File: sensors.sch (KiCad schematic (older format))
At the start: 14 parts, among them Q1901 FDV301N, Q1902 FDV301N, U1901 RPR-0521RS, U1902 ICM-20948

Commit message: Modify the boot config/boot mode pins and switch such that only eMMC and USB (serial downloader) are boot options due to the uSD being attached to the USB<->SD bridge chip, add OV5460 notes about using the internal DVDD 1.5V regulator
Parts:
- renumbered C1901 to C2001, C1902 to C2002, C1903 to C2003, C1904 to C2004, C1905 to C2005, C1906 to C2006, Q1901 to Q2001, Q1902 to Q2002, R1901 to R2001, R1902 to R2002, R1903 to R2003, R1904 to R2004, U1901 to U2001, U1902 to U2002
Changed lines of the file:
@@
 $EndDescr
 $Comp
-L R R1902
+L R R2002
 U 1 1 5B0661C0
 P 4150 2150
-F 0 "R1902" V 4230 2150 50  0000 C CNN
+F 0 "R2002" V 4230 2150 50  0000 C CNN
 F 1 "22" V 4150 2150 50  0000 C CNN
 F 2 "Resistors_SMD:R_0603" V 4080 2150 50  0001 C CNN
@@
 $EndComp
 $Comp
-L C C1903
+L C C2003
 U 1 1 5B067A54
 P 4700 3150
-F 0 "C1903" H 4725 3250 50  0000 L CNN
+F 0 "C2003" H 4725 3250 50  0000 L CNN
 F 1 "100nF" H 4725 3050 50  0000 L CNN
 F 2 "" H 4738 3000 50  0001 C CNN
@@
 	4400 3500 4350 3500
 $Comp
-L GND #PWR0311
+L GND #PWR0305
 U 1 1 5B067AE0
 P 4600 3400
-F 0 "#PWR0311" H 4600 3150 50  0001 C CNN
+F 0 "#PWR0305" H 4600 3150 50  0001 C CNN
 F 1 "GND" H 4600 3250 50  0000 C CNN
 F 2 "" H 4600 3400 50  0001 C CNN
@@
 	4700 2950 4350 2950
 $Comp
-L GND #PWR0312
+L GND #PWR0306
 U 1 1 5B068781
 P 3800 4000
-F 0 "#PWR0312" H 3800 3750 50  0001 C CNN
+F 0 "#PWR0306" H 3800 3750 50  0001 C CNN
 F 1 "GND" H 3800 3850 50  0000 C CNN
 F 2 "" H 3800 4000 50  0001 C CNN
@@
 	3800 4000 3800 3950
 $Comp
-L GND #PWR0313
+L GND #PWR0307
 U 1 1 5B068863
 P 3600 2550
-F 0 "#PWR0313" H 3600 2300 50  0001 C CNN
+F 0 "#PWR0307" H 3600 2300 50  0001 C CNN
 F 1 "GND" H 3600 2400 50  0000 C CNN
 F 2 "" H 3600 2550 50  0001 C CNN
@@
 Connection ~ 3800 2150
 $Comp
-L 3V3_P #PWR0314
+L 3V3_P #PWR0308
 U 1 1 5B0689D2
 P 4700 2100
-F 0 "#PWR0314" H 4700 1950 50  0001 C CNN
+F 0 "#PWR0308" H 4700 1950 50  0001 C CNN
 F 1 "3V3_P" H 4700 2240 50  0000 C CNN
 F 2 "" H 4700 2100 50  0001 C CNN
@@
 	3250 2950 2750 2950
 $Comp
-L 3V3_P #PWR0315
+L 3V3_P #PWR0309
 U 1 1 5B069B9B
 P 3200 2900
-F 0 "#PWR0315" H 3200 2750 50  0001 C CNN
+F 0 "#PWR0309" H 3200 2750 50  0001 C CNN
 F 1 "3V3_P" H 3200 3040 50  0000 C CNN
 F 2 "" H 3200 2900 50  0001 C CNN
@@
 Proximity & Ambient Light
 $Comp
-L RPR-0521RS U1901
+L RPR-0521RS U2001
 U 1 1 5B0DE7C1
 P 3800 3300
-F 0 "U1901" H 3600 3800 60  0000 C CNN
+F 0 "U2001" H 3600 3800 60  0000 C CNN
 F 1 "RPR-0521RS" H 4100 3800 60  0000 C CNN
 F 2 "dvk-mx8m-bsb:RPR-0521RS" H 3800 3150 60  0001 C CNN
@@
 $EndComp
 $Comp
-L C C1902
+L C C2002
 U 1 1 5B0E0E47
 P 4500 3150
-F 0 "C1902" H 4525 3250 50  0000 L CNN
+F 0 "C2002" H 4525 3250 50  0000 L CNN
 F 1 "100nF" H 4525 3050 50  0000 L CNN
 F 2 "" H 4538 3000 50  0001 C CNN
@@
 	7450 2400 6800 2400
 $Comp
-L GND #PWR0316
+L GND #PWR0310
 U 1 1 5B0EFE3A
 P 7300 2650
-F 0 "#PWR0316" H 7300 2400 50  0001 C CNN
+F 0 "#PWR0310" H 7300 2400 50  0001 C CNN
 F 1 "GND" H 7300 2500 50  0000 C CNN
 F 2 "" H 7300 2650 50  0001 C CNN
@@
 Reference:\nhttps://store.invensense.com/datasheets/invensense/\nAN-IVS-0001EVB-00%20v1%202.pdf
 $Comp
-L C C1906
+L C C2006
 U 1 1 5B0F1B79
 P 9450 2300
-F 0 "C1906" H 9475 2400 50  0000 L CNN
+F 0 "C2006" H 9475 2400 50  0000 L CNN
 F 1 "100nF" H 9475 2200 50  0000 L CNN
 F 2 "" H 9488 2150 50  0001 C CNN
@@
 	8750 2100 9450 2100
 $Comp
-L GND #PWR0317
+L GND #PWR0311
 U 1 1 5B0F1D3B
 P 9450 2500
-F 0 "#PWR0317" H 9450 2250 50  0001 C CNN
+F 0 "#PWR0311" H 9450 2250 50  0001 C CNN
 F 1 "GND" H 9450 2350 50  0000 C CNN
 F 2 "" H 9450 2500 50  0001 C CNN
@@
 	9450 2500 9450 2450
 $Comp
-L 3V3_P #PWR0318
+L 3V3_P #PWR0312
 U 1 1 5B0F3735
 P 9450 2050
-F 0 "#PWR0318" H 9450 1900 50  0001 C CNN
+F 0 "#PWR0312" H 9450 1900 50  0001 C CNN
 F 1 "3V3_P" H 9450 2190 50  0000 C CNN
 F 2 "" H 9450 2050 50  0001 C CNN
@@
 Connection ~ 9450 2100
 $Comp
-L 1V8_P #PWR0319
+L 1V8_P #PWR0313
 U 1 1 5B0F45AF
 P 6700 2050
-F 0 "#PWR0319" H 6700 1900 50  0001 C CNN
+F 0 "#PWR0313" H 6700 1900 50  0001 C CNN
 F 1 "1V8_P" H 6700 2190 50  0000 C CNN
 F 2 "" H 6700 2050 50  0001 C CNN
@@
 $EndComp
 $Comp
-L C C1904
+L C C2004
 U 1 1 5B0F45D3
 P 6700 2450
-F 0 "C1904" H 6725 2550 50  0000 L CNN
+F 0 "C2004" H 6725 2550 50  0000 L CNN
 F 1 "100nF" H 6725 2350 50  0000 L CNN
 F 2 "" H 6738 2300 50  0001 C CNN
@@
 $EndComp
 $Comp
-L GND #PWR0320
+L GND #PWR0314
 U 1 1 5B0F4626
 P 6700 2650
-F 0 "#PWR0320" H 6700 2400 50  0001 C CNN
+F 0 "#PWR0314" H 6700 2400 50  0001 C CNN
 F 1 "GND" H 6700 2500 50  0000 C CNN
 F 2 "" H 6700 2650 50  0001 C CNN
@@
 	6700 2650 6700 2600
 $Comp
-L C C1905
+L C C2005
 U 1 1 5B0FA115
 P 9050 2800
-F 0 "C1905" H 9075 2900 50  0000 L CNN
+F 0 "C2005" H 9075 2900 50  0000 L CNN
 F 1 "100nF" H 9075 2700 50  0000 L CNN
 F 2 "" H 9088 2650 50  0001 C CNN
@@
 $EndComp
 $Comp
-L GND #PWR0321
+L GND #PWR0315
 U 1 1 5B0FA198
 P 9050 3000
-F 0 "#PWR0321" H 9050 2750 50  0001 C CNN
+F 0 "#PWR0315" H 9050 2750 50  0001 C CNN
 F 1 "GND" H 9050 2850 50  0000 C CNN
 F 2 "" H 9050 3000 50  0001 C CNN
@@
 	9050 3000 9050 2950
 $Comp
-L 1V8_P #PWR0322
+L 1V8_P #PWR0316
 U 1 1 5B0FDFE1
 P 8800 2050
-F 0 "#PWR0322" H 8800 1900 50  0001 C CNN
+F 0 "#PWR0316" H 8800 1900 50  0001 C CNN
 F 1 "1V8_P" H 8800 2190 50  0000 C CNN
 F 2 "" H 8800 2050 50  0001 C CNN
@@
 	7450 2500 7400 2500
 $Comp
-L GND #PWR0323
+L GND #PWR0317
 U 1 1 5B105474
 P 8850 2650
-F 0 "#PWR0323" H 8850 2400 50  0001 C CNN
+F 0 "#PWR0317" H 8850 2400 50  0001 C CNN
 F 1 "GND" H 8850 2500 50  0000 C CNN
 F 2 "" H 8850 2650 50  0001 C CNN
@@
 I2C's VIH=1.8V
 $Comp
-L Q_NMOS_SGD Q1901
+L Q_NMOS_SGD Q2001
 U 1 1 5B11E6E9
 P 4500 5450
-F 0 "Q1901" V 4750 5350 50  0000 L CNN
+F 0 "Q2001" V 4750 5350 50  0000 L CNN
 F 1 "FDV301N" V 4850 5300 50  0000 L CNN
 F 2 "" H 4700 5550 50  0001 C CNN
@@
 $EndComp
 $Comp
-L 1V8_P #PWR0324
+L 1V8_P #PWR0318
 U 1 1 5B11E6F7
 P 4750 5100
-F 0 "#PWR0324" H 4750 4950 50  0001 C CNN
+F 0 "#PWR0318" H 4750 4950 50  0001 C CNN
 F 1 "1V8_P" H 4750 5240 50  0000 C CNN
 F 2 "" H 4750 5100 50  0001 C CNN
@@
 Connection ~ 4750 5150
 $Comp
-L Q_NMOS_SGD Q1902
+L Q_NMOS_SGD Q2002
 U 1 1 5B11E705
 P 6800 5450
-F 0 "Q1902" V 7050 5350 50  0000 L CNN
+F 0 "Q2002" V 7050 5350 50  0000 L CNN
 F 1 "FDV301N" V 7150 5300 50  0000 L CNN
 F 2 "" H 7000 5550 50  0001 C CNN
@@
 	3850 5550 4300 5550
 $Comp
-L 1V8_P #PWR0325
+L 1V8_P #PWR0319
 U 1 1 5B11E71E
 P 7050 5100
-F 0 "#PWR0325" H 7050 4950 50  0001 C CNN
+F 0 "#PWR0319" H 7050 4950 50  0001 C CNN
 F 1 "1V8_P" H 7050 5240 50  0000 C CNN
 F 2 "" H 7050 5100 50  0001 C CNN
@@
 I2C1_SCL
 $Comp
-L PWR_FLAG #FLG0326
+L PWR_FLAG #FLG0320
 U 1 1 5B123465
 P 3800 2100
-F 0 "#FLG0326" H 3800 2175 50  0001 C CNN
+F 0 "#FLG0320" H 3800 2175 50  0001 C CNN
 F 1 "PWR_FLAG" H 3800 2250 50  0000 C CNN
 F 2 "" H 3800 2100 50  0001 C CNN
@@
 $EndBitmap
 $Comp
-L ICM-20948 U1902
+L ICM-20948 U2002
 U 1 1 5AF6DE9D
 P 8100 2650
-F 0 "U1902" H 7750 3350 60  0000 R CNN
+F 0 "U2002" H 7750 3350 60  0000 R CNN
 F 1 "ICM-20948" H 8550 3350 60  0000 R CNN
 F 2 "" H 8100 2600 60  0001 C CNN
@@
 	7400 3550 7400 2500
 $Comp
-L R R1901
+L R R2001
 U 1 1 5B32CA87
 P 3200 3250
-F 0 "R1901" H 3375 3300 50  0000 C CNN
+F 0 "R2001" H 3375 3300 50  0000 C CNN
 F 1 "10k" H 3325 3200 50  0000 C CNN
 F 2 "Resistors_SMD:R_0603" V 3130 3250 50  0001 C CNN
@@
 $EndComp
 $Comp
-L R R1903
+L R R2003
 U 1 1 5B32E4D4
 P 4750 5350
-F 0 "R1903" H 4925 5400 50  0000 C CNN
+F 0 "R2003" H 4925 5400 50  0000 C CNN
 F 1 "10k" H 4875 5300 50  0000 C CNN
 F 2 "Resistors_SMD:R_0603" V 4680 5350 50  0001 C CNN
@@
 $EndComp
 $Comp
-L R R1904
+L R R2004
 U 1 1 5B32E554
 P 7050 5350
-F 0 "R1904" H 7225 5400 50  0000 C CNN
+F 0 "R2004" H 7225 5400 50  0000 C CNN
 F 1 "10k" H 7175 5300 50  0000 C CNN
 F 2 "Resistors_SMD:R_0603" V 6980 5350 50  0001 C CNN
@@
 $EndComp
 $Comp
-L C C1901
+L C C2001
 U 1 1 5B0BFB2C
 P 3600 2350
-F 0 "C1901" H 3350 2450 50  0000 L CNN
+F 0 "C2001" H 3350 2450 50  0000 L CNN
 F 1 "10uF" H 3400 2250 50  0000 L CNN
 F 2 "Capacitors_SMD:C_0603" H 3638 2200 50  0001 C CNN

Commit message: Use the 2SK3018 NMOS for all low-current applications such as level-shifting
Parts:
- removed Q2001, Q2002: FDV301N, symbol Q_NMOS_SGD
- added Q2001, Q2002: 2SK3018, symbol Q_NMOS_GSD
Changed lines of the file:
@@
 I2C's VIH=1.8V
-$Comp
-L Q_NMOS_SGD Q2001
-U 1 1 5B11E6E9
-P 4500 5450
-F 0 "Q2001" V 4750 5350 50  0000 L CNN
-F 1 "FDV301N" V 4850 5300 50  0000 L CNN
-F 2 "" H 4700 5550 50  0001 C CNN
-F 3 "" H 4500 5450 50  0001 C CNN
-	1    4500 5450
-	0    -1   1    0
-$EndComp
 $Comp
 L 1V8_P #PWR0340
@@
 	4500 5150 4750 5150
 Connection ~ 4750 5150
-$Comp
-L Q_NMOS_SGD Q2002
-U 1 1 5B11E705
-P 6800 5450
-F 0 "Q2002" V 7050 5350 50  0000 L CNN
-F 1 "FDV301N" V 7150 5300 50  0000 L CNN
-F 2 "" H 7000 5550 50  0001 C CNN
-F 3 "" H 6800 5450 50  0001 C CNN
-	1    6800 5450
-	0    -1   1    0
-$EndComp
 Wire Wire Line
 	7000 5550 7750 5550
@@
 	1    0    0    -1
 $EndComp
+$Comp
+L Q_NMOS_GSD Q2001
+U 1 1 5B5A1F96
+P 4500 5450
+F 0 "Q2001" V 4725 5325 50  0000 L CNN
+F 1 "2SK3018" V 4800 5275 50  0000 L CNN
+F 2 "" H 4700 5550 50  0001 C CNN
+F 3 "http://www.mccsemi.com/up_pdf/2SK3018(SOT-323).pdf" H 4500 5450 50  0001 C CNN
+F 4 "Micro Commercial Co" V 4500 5450 60  0001 C CNN "MFG Name"
+F 5 "2SK3018-TP" V 4500 5450 60  0001 C CNN "MFG Part Num"
+F 6 "833-2SK3018-TP" V 4500 5450 60  0001 C CNN "Distrib PN"
+F 7 "https://www.mouser.com/ProductDetail/Micro-Commercial-Components-MCC/2SK3018-TP?qs=sGAEpiMZZMtI26rxh1qzjnDHXOVLFYvgyLpQIEHdJp0%3d" V 4500 5450 60  0001 C CNN "Distrib Link"
+F 8 "-" V 4500 5450 60  0001 C CNN "Tolerance"
+F 9 "https://www.digikey.com/product-detail/en/micro-commercial-co/2SK3018-TP/2SK3018-TPMSCT-ND/6616131" V 4500 5450 60  0001 C CNN "Others"
+	1    4500 5450
+	0    -1   1    0
+$EndComp
+$Comp
+L Q_NMOS_GSD Q2002
+U 1 1 5B5A20E4
+P 6800 5450
+F 0 "Q2002" V 7025 5325 50  0000 L CNN
+F 1 "2SK3018" V 7100 5275 50  0000 L CNN
+F 2 "" H 7000 5550 50  0001 C CNN
+F 3 "http://www.mccsemi.com/up_pdf/2SK3018(SOT-323).pdf" H 6800 5450 50  0001 C CNN
+F 4 "Micro Commercial Co" V 6800 5450 60  0001 C CNN "MFG Name"
+F 5 "2SK3018-TP" V 6800 5450 60  0001 C CNN "MFG Part Num"
+F 6 "833-2SK3018-TP" V 6800 5450 60  0001 C CNN "Distrib PN"
+F 7 "https://www.mouser.com/ProductDetail/Micro-Commercial-Components-MCC/2SK3018-TP?qs=sGAEpiMZZMtI26rxh1qzjnDHXOVLFYvgyLpQIEHdJp0%3d" V 6800 5450 60  0001 C CNN "Distrib Link"
+F 8 "-" V 6800 5450 60  0001 C CNN "Tolerance"
+F 9 "https://www.digikey.com/product-detail/en/micro-commercial-co/2SK3018-TP/2SK3018-TPMSCT-ND/6616131" V 6800 5450 60  0001 C CNN "Others"
+	1    6800 5450
+	0    -1   1    0
+$EndComp
 $EndSCHEMATC

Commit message: Replace ICM-20948 IMU with the LSM90S1, replace RPR-0521RS prox+ambient light sensor with the VCNL4040
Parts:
- removed Q2001, Q2002: 2SK3018, symbol Q_NMOS_GSD
- removed R2003, R2004: 10k, Resistors_SMD:R_0603, symbol R
- removed U2001: RPR-0521RS, dvk-mx8m-bsb:RPR-0521RS, symbol RPR-0521RS
- removed U2002: ICM-20948, symbol ICM-20948
- added C2007: 100nF, Capacitors_SMD:C_0603, symbol C
- added U2001: VCNL4040, symbol VCNL4040
- added U2002: LSM9DS1, Housings_LGA:LGA-24L_3x3.5mm_Pitch0.43mm, symbol LSM9DS1
- added U2003: 74LVC1G332, http://www.ti.com/lit/ds/symlink/sn74lvc1g332.pdf, symbol SN74LVC1G332
- C2001: value 10uF -> 470nF
- C2002: value 100nF -> 10nF; footprint (none) -> Capacitors_SMD:C_0603
- C2003: value 100nF -> 2.2uF; footprint (none) -> Capacitors_SMD:C_0603
- C2004, C2006: footprint (none) -> Capacitors_SMD:C_0603
- C2005: value 100nF -> 10uF; footprint (none) -> Capacitors_SMD:C_0603
- R2002: value 22 -> 0
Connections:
- net labels added: INT1, INT2, INT_M
- net labels removed: 1V8_P, I2C1_SCL_1V8, I2C1_SDA_1V8
- wire segments 56 -> 60
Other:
- note added: "0X1E"
- note added: "0x6B"
- note added: "Note:\nI2C 2.2kΩ pull-up suggested\ncheck input capacitance & rise time"
- note added: "Ref Fig. 21"
- note added: "Reference:\nhttp://www.st.com/en/evaluation-tools/steval-mki159v1.html"
- note added: "Reference:\nhttps://www.vishay.com/docs/84307/designingvcnl4040.pdf\nhttp://www.vishay.com/docs/84931/vcnl4040sensorboardfiles.pdf"
- note added: "SDO_A/G Address\n 1 0x6B\n 0 0x6A"
- note added: "SDO_M Address\n 1 0x1E\n 0 0x1C"
- note added: "must guarantee 1nF value\nunder 11V bias condition"
- note added: "≤10%\n 16V"
- note removed: ""FSYNC - Connect to GND if unused""
- note removed: "AD0 sets the slave address's LSB (110100X)"
- note removed: "I2C's VIH=1.8V"
- note removed: "INT1_ACTL sets if IMU_INT\nis active-high or active-low"
- note removed: "Reference:\nhttp://www.rohm.com/web/global/sensor-shield-support/ps-als-sensor"
- note removed: "Reference:\nhttps://store.invensense.com/datasheets/invensense/\nAN-IVS-0001EVB-00%20v1%202.pdf"
- moved on the sheet: C2001, C2003

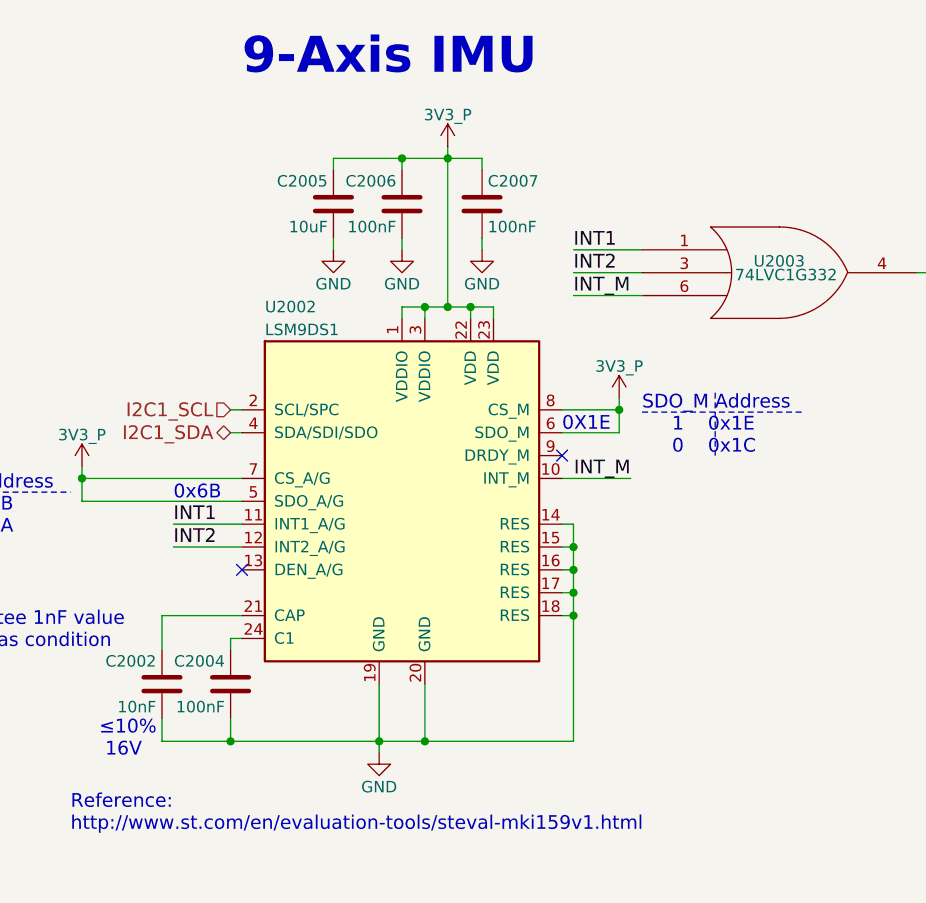
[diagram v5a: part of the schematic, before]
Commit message: Add bypass caps to logic gates used with the W_DISABLE and the 9-axis IMU's INT pins
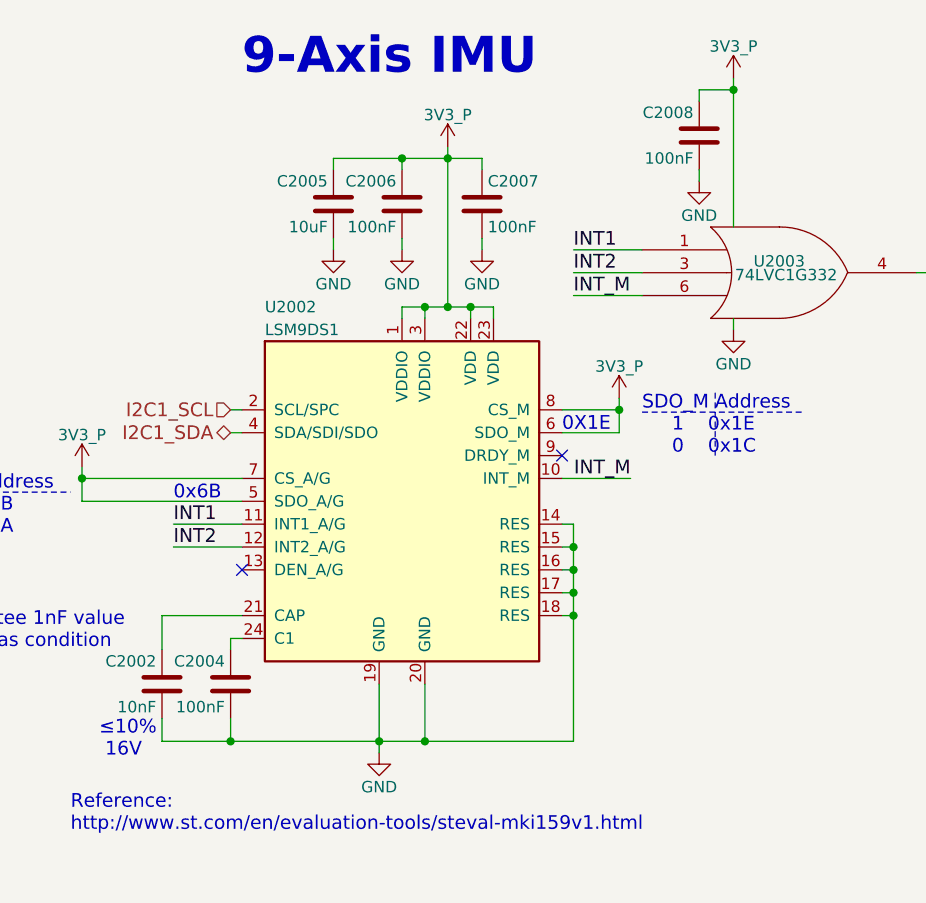
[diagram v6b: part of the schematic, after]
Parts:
- added C2008: 100nF, Capacitors_SMD:C_0603, symbol C
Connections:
- net Vcc is gone; now on net 3V3_P: U2003.5 (Vcc)
- net 3V3_P: now also C2008.1
- net GND: now also C2008.2
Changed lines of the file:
@@
 $EndComp
 $Comp
-L GND #PWR0327
+L GND #PWR2005
 U 1 1 5B067AE0
 P 4550 3450
-F 0 "#PWR0327" H 4550 3200 50  0001 C CNN
+F 0 "#PWR2005" H 4550 3200 50  0001 C CNN
 F 1 "GND" H 4550 3300 50  0000 C CNN
 F 2 "" H 4550 3450 50  0001 C CNN
@@
 $EndComp
 $Comp
-L GND #PWR0328
+L GND #PWR2003
 U 1 1 5B068781
 P 3800 4100
-F 0 "#PWR0328" H 3800 3850 50  0001 C CNN
+F 0 "#PWR2003" H 3800 3850 50  0001 C CNN
 F 1 "GND" H 3800 3950 50  0000 C CNN
 F 2 "" H 3800 4100 50  0001 C CNN
@@
 $EndComp
 $Comp
-L GND #PWR0329
+L GND #PWR2002
 U 1 1 5B068863
 P 3600 2650
-F 0 "#PWR0329" H 3600 2400 50  0001 C CNN
+F 0 "#PWR2002" H 3600 2400 50  0001 C CNN
 F 1 "GND" H 3600 2500 50  0000 C CNN
 F 2 "" H 3600 2650 50  0001 C CNN
@@
 $EndComp
 $Comp
-L 3V3_P #PWR0330
+L 3V3_P #PWR2004
 U 1 1 5B0689D2
 P 4550 2200
-F 0 "#PWR0330" H 4550 2050 50  0001 C CNN
+F 0 "#PWR2004" H 4550 2050 50  0001 C CNN
 F 1 "3V3_P" H 4550 2350 50  0000 C CNN
 F 2 "" H 4550 2200 50  0001 C CNN
@@
 $EndComp
 $Comp
-L 3V3_P #PWR0331
+L 3V3_P #PWR2001
 U 1 1 5B069B9B
 P 2600 3150
-F 0 "#PWR0331" H 2600 3000 50  0001 C CNN
+F 0 "#PWR2001" H 2600 3000 50  0001 C CNN
 F 1 "3V3_P" H 2600 3290 50  0000 C CNN
 F 2 "" H 2600 3150 50  0001 C CNN
@@
 $EndComp
 $Comp
-L PWR_FLAG #FLG0332
+L PWR_FLAG #FLG2001
 U 1 1 5B13CB3F
 P 3800 2200
-F 0 "#FLG0332" H 3800 2275 50  0001 C CNN
+F 0 "#FLG2001" H 3800 2275 50  0001 C CNN
 F 1 "PWR_FLAG" H 3800 2350 50  0000 C CNN
 F 2 "" H 3800 2200 50  0001 C CNN
@@
 $EndComp
 $Comp
-L GND #PWR0333
+L GND #PWR2008
 U 1 1 5B15906B
 P 8200 4450
-F 0 "#PWR0333" H 8200 4200 50  0001 C CNN
+F 0 "#PWR2008" H 8200 4200 50  0001 C CNN
 F 1 "GND" H 8200 4300 50  0000 C CNN
 F 2 "" H 8200 4450 50  0001 C CNN
@@
 $EndComp
 $Comp
-L 3V3_P #PWR0334
+L 3V3_P #PWR2010
 U 1 1 5B15B71F
 P 8500 1800
-F 0 "#PWR0334" H 8500 1650 50  0001 C CNN
+F 0 "#PWR2010" H 8500 1650 50  0001 C CNN
 F 1 "3V3_P" H 8500 1940 50  0000 C CNN
 F 2 "" H 8500 1800 50  0001 C CNN
@@
 $EndComp
 $Comp
-L GND #PWR0335
+L GND #PWR2011
 U 1 1 5B15B942
 P 8650 2250
-F 0 "#PWR0335" H 8650 2000 50  0001 C CNN
+F 0 "#PWR2011" H 8650 2000 50  0001 C CNN
 F 1 "GND" H 8650 2100 50  0000 C CNN
 F 2 "" H 8650 2250 50  0001 C CNN
@@
 $EndComp
 $Comp
-L GND #PWR0336
+L GND #PWR2009
 U 1 1 5B15B987
 P 8300 2250
-F 0 "#PWR0336" H 8300 2000 50  0001 C CNN
+F 0 "#PWR2009" H 8300 2000 50  0001 C CNN
 F 1 "GND" H 8300 2100 50  0000 C CNN
 F 2 "" H 8300 2250 50  0001 C CNN
@@
 $EndComp
 $Comp
-L GND #PWR0337
+L GND #PWR2007
 U 1 1 5B15BC52
 P 8000 2250
-F 0 "#PWR0337" H 8000 2000 50  0001 C CNN
+F 0 "#PWR2007" H 8000 2000 50  0001 C CNN
 F 1 "GND" H 8000 2100 50  0000 C CNN
 F 2 "" H 8000 2250 50  0001 C CNN
@@
 INT_M
 $Comp
-L 3V3_P #PWR0338
+L 3V3_P #PWR2006
 U 1 1 5B176622
 P 6900 3200
-F 0 "#PWR0338" H 6900 3050 50  0001 C CNN
+F 0 "#PWR2006" H 6900 3050 50  0001 C CNN
 F 1 "3V3_P" H 6900 3340 50  0000 C CNN
 F 2 "" H 6900 3200 50  0001 C CNN
@@
 $EndComp
 $Comp
-L 3V3_P #PWR0339
+L 3V3_P #PWR2012
 U 1 1 5B1766DE
 P 9250 2900
-F 0 "#PWR0339" H 9250 2750 50  0001 C CNN
+F 0 "#PWR2012" H 9250 2750 50  0001 C CNN
 F 1 "3V3_P" H 9250 3040 50  0000 C CNN
 F 2 "" H 9250 2900 50  0001 C CNN
@@
 Connection ~ 7550 4400
 Wire Wire Line
-	7250 4300 7250 4400
+	7250 4400 7250 4300
 Wire Wire Line
 	7250 3850 7250 4000
@@
 Wire Wire Line
 	8000 2200 8000 2250
+$Comp
+L GND #PWR2015
+U 1 1 5B0CAE93
+P 9750 2600
+F 0 "#PWR2015" H 9750 2350 50  0001 C CNN
+F 1 "GND" H 9750 2450 50  0000 C CNN
+F 2 "" H 9750 2600 50  0001 C CNN
+F 3 "" H 9750 2600 50  0001 C CNN
+	1    9750 2600
+	1    0    0    -1
+$EndComp
+Wire Wire Line
+	9750 2550 9750 2600
+$Comp
+L 3V3_P #PWR2014
+U 1 1 5B0CB162
+P 9750 1500
+F 0 "#PWR2014" H 9750 1350 50  0001 C CNN
+F 1 "3V3_P" H 9750 1640 50  0000 C CNN
+F 2 "" H 9750 1500 50  0001 C CNN
+F 3 "" H 9750 1500 50  0001 C CNN
+	1    9750 1500
+	1    0    0    -1
+$EndComp
+Wire Wire Line
+	9750 1500 9750 2150
+$Comp
+L C C2008
+U 1 1 5B0EBD64
+P 9600 1750
+F 0 "C2008" H 9625 1850 50  0000 L CNN
+F 1 "100nF" H 9625 1650 50  0000 L CNN
+F 2 "Capacitors_SMD:C_0603" H 9638 1600 50  0001 C CNN
+F 3 "" H 9600 1750 50  0001 C CNN
+	1    9600 1750
+	-1   0    0    -1
+$EndComp
+$Comp
+L GND #PWR2013
+U 1 1 5B0EBDA7
+P 9600 1950
+F 0 "#PWR2013" H 9600 1700 50  0001 C CNN
+F 1 "GND" H 9600 1800 50  0000 C CNN
+F 2 "" H 9600 1950 50  0001 C CNN
+F 3 "" H 9600 1950 50  0001 C CNN
+	1    9600 1950
+	1    0    0    -1
+$EndComp
+Wire Wire Line
+	9600 1600 9600 1550
+Wire Wire Line
+	9600 1550 9750 1550
+Connection ~ 9750 1550
+Wire Wire Line
+	9600 1900 9600 1950
 $EndSCHEMATC
